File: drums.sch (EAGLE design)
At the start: 210 parts, among them IC1 4051N, IC3 7812T, IC5 OPA2134P, IC6 OPA4130P, IC7 LM2574HVN-5.0, IC8 74LS595N, J2 UBBS-4R-D14-4D

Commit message: added hihats, buncha stuff
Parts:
- added C49, C52, C56, C57, C64, C65: 15n, dan:C-US050-025X075
- added C50, C51: 10n, dan:C-US050-025X075
- added C53, C54: 12n, dan:C-US050-025X075
- added C55: 3.3n, dan:C-US050-025X075
- added C58, C62: 1u, dan:CPOL-USE2-5
- added C59: np, dan:C-US050-025X075
- added C60: .47u, dan:CPOL-USE2-5
- added C61: 5.6n, dan:C-US050-025X075
- added C63: np, dan:CPOL-USE2-5
- added C66: 33u, dan:CPOL-USE2-5
- added CHDECAY: 50k, dan:US-EVUF2J
- added D13, D14, D15, D16: 1N4148DO35-7, dan:1N4148DO35-7
- added HATFILTER, VOLUME: 10k, dan:US-EVUF2J
- added HATSLEVEL, OHDECAY1: 500k, dan:US-EVUF2J
- added IC2: 4584N, dan:4584N
- added IC9: OPA4130P, dan:OPA4130P
- added JP7, JP8: (no value), dan:PINHD-2X6
- added R101, R102, R103, R104, R105, R24: 150k, dan:R-US_0207/2V
- added R106: 1k, dan:R-US_0207/2V
- added R107, R131, R132, R133: 33k, dan:R-US_0207/2V
- added R108, R109: 100, dan:R-US_0207/2V
- added R110: 1M, dan:R-US_0207/2V
- added R111, R115, R123, R127: 22k, dan:R-US_0207/2V
- added R112, R130: 220, dan:R-US_0207/2V
- added R113, R118, R121, R126: 4.7k, dan:R-US_0207/2V
- added R114, R116, R117, R120, R122, R124, R125: 10k, dan:R-US_0207/2V
- added R119, R16, R20: 330k, dan:R-US_0207/2V
- added R128, R129, R134, R135, R136: 100k, dan:R-US_0207/2V
- added R137: 82k, dan:R-US_0207/2V
- added R19, R21: 470k, dan:R-US_0207/2V
- added R22, R23: 560k, dan:R-US_0207/2V
- added U$14, U$16, U$18, U$19, U$20, U$21, U$22: 2N3904_, dan:2N3904_
- added U$15, U$17: 2N3906_, dan:2N3906_
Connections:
- removed net N$132: JP1.6
- removed net N$138: JP2.4
- removed net N$144: JP2.3
- removed net N$145: JP2.5
- removed net N$2: R2.2, U$1.3.3V
- removed net N$32: JP1.3
- removed net N$35: R18.1, U$1.1/TX1/T
- removed net N$48: JP1.11
- removed net N$50: JP1.4
- new net CHDEC2A: CHDECAY.E
- new net CHDEC2B: C64.1, D13.A, JP2.5
- new net CHDEC3B: C60.+, D14.C, JP2.6
- new net CHDECA: CHDECAY.A, CHDECAY.S, JP1.4, JP1.6
- new net CHDECB: JP2.4, R119.2
- new net D+B: J2.D+, JP2.10
- new net D-B: J2.D-, JP2.11
- new net HATLEV2A: HATSLEVEL.A, JP1.9
- new net HATLEV2B: C66.-, JP2.9
- new net HATLEVA: HATSLEVEL.E, HATSLEVEL.S, JP1.8
- new net HATLEVB: IC9B.OUT, JP2.8, R134.1
- new net HFILTA: HATFILTER.E, JP1.3
- new net HFILTB: JP2.3, R108.2
- new net MIDRXA: JP1.12, U$1.0/RX1/T
- new net MIDRXB: JP2.12, OK1.VO, R2.1
- new net MIDTXA: JP1.5, U$1.1/TX1/T
- new net MIDTXB: JP2.7, R18.1
- new net N$106: IC2F.O, R105.2, R23.1
- new net N$107: C54.1, IC2F.I, R23.2
- new net N$109: C58.+, R110.2, U$14.B
- new net N$110: C55.2, R101.1, R102.1, R103.1, R104.1, R105.1, R106.1, R24.1
- new net N$143: C55.1, R107.2
- new net N$149: C56.2, IC9A.-IN, R107.1, R137.2
- new net N$150: C56.1, C57.2, R108.1
- new net N$151: C57.1, C58.-, IC9A.OUT, R137.1
- new net N$152: R109.1, U$14.E
- new net N$155: C59.1, D13.C, D15.C, U$14.C
- new net N$156: JP8.12
- new net N$158: D14.A, R112.1
- new net N$159: R113.1, R114.2, U$15.B
- new net N$161: R111.2, R112.2, U$15.C
- new net N$162: R113.2, R117.1, R118.1, U$15.E
- new net N$163: R114.1, U$16.C
- new net N$164: R115.1, R116.1, U$16.B
- new net N$168: D16.A, R127.2, U$17.C
- new net N$169: R121.1, R122.2, U$17.B
- new net N$170: R121.2, R125.1, R126.1, U$17.E
- new net N$171: R122.1, U$18.C
- new net N$173: R123.1, R124.1, U$18.B
- new net N$176: R120.2, R127.1, U$19.B
- new net N$177: C61.1, R128.2, U$19.C
- new net N$178: C65.1, D15.A, R133.1
- new net N$179: R128.1, U$20.B
- new net N$180: C63.+, R129.2, U$20.C, U$21.C
- new net N$181: D16.C, R130.2
- new net N$183: R131.1, U$22.B
- new net N$184: R132.2, R133.2, U$22.E
- new net N$185: R119.1, U$21.B
- new net N$187: C64.2, R136.2
- new net N$188: C65.2, R135.2
- new net N$189: C66.+, IC9B.-IN, R134.2, R135.1, R136.1
- new net N$31: C52.1, IC2D.I, R21.2
- new net N$49: IC2D.O, R103.2, R21.1
- new net N$67: IC2A.O, R16.1, R24.2
- new net N$71: C49.1, IC2A.I, R16.2
- new net N$74: C50.1, IC2B.I, R19.2
- new net N$75: IC2B.O, R101.2, R19.1
- new net N$79: IC2C.O, R102.2, R20.1
- new net N$80: C51.1, IC2C.I, R20.2
- new net N$85: C53.1, IC2E.I, R22.2
- new net N$86: IC2E.O, R104.2, R22.1
- new net OHDECA: JP7.2, OHDECAY1.A
- new net OHDECB: C62.+, JP8.2, R129.1, R130.1, R131.2
- new net T5B: JP8.3, R115.2
- new net T6B: JP8.4, R123.2
- new net T7B: JP8.5, R118.2, R126.2
- net +12V: now also IC9A.V+, R110.1, R117.2, R125.2, U$22.C
- net -12V: now also IC9A.V-
- net 3.3V: now also IC1P.VCC, IC2P.VDD, U$1.3.3V; no longer OK1.VO, R2.1, U$1.0/RX1/T
- net 5V: now also IC8P.VCC, R2.2
- net D+A: now also JP1.10; no longer J2.D+
- net D-A: now also JP1.11; no longer J2.D-
- net GND: now also C49.2, C50.2, C51.2, C52.2, C53.2, C54.2, C59.2, C60.-, C61.2, C62.-, C63.-, HATFILTER.A, HATFILTER.S, IC1P.GND, IC1P.VEE, IC2P.VSS, IC8P.GND, IC9A.+IN, IC9B.+IN, JP1.7, JP7.1, JP8.1, OHDECAY1.E, OHDECAY1.S, R106.2, R109.2, R111.1, R116.2, R120.1, R124.2, R132.1, U$16.E, U$18.E, U$19.E, U$20.E, U$21.E
- net N$134: now also JP8.7; no longer JP1.8
- net N$135: now also JP8.9; no longer JP1.10
- net N$136: now also JP8.11; no longer JP1.12
- net N$139: now also JP7.6; no longer JP2.6
- net N$140: now also JP7.8; no longer JP2.8
- net N$141: now also JP7.10; no longer JP2.10
- net N$142: now also JP7.12; no longer JP2.12
- net N$146: now also JP8.6; no longer JP2.7
- net N$147: now also JP8.8; no longer JP2.9
- net N$148: now also JP8.10; no longer JP2.11
- net N$38: now also JP7.7; no longer JP1.5
- net N$39: now also JP7.9; no longer JP1.7
- net N$47: now also JP7.11; no longer JP1.9
- net T5: now also JP7.3
- net T6: now also JP7.4
- net T7: now also JP7.5
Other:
- note added: "maybe patch in noise here too"
- moved on the sheet: C7, D+, D-, R2, R25

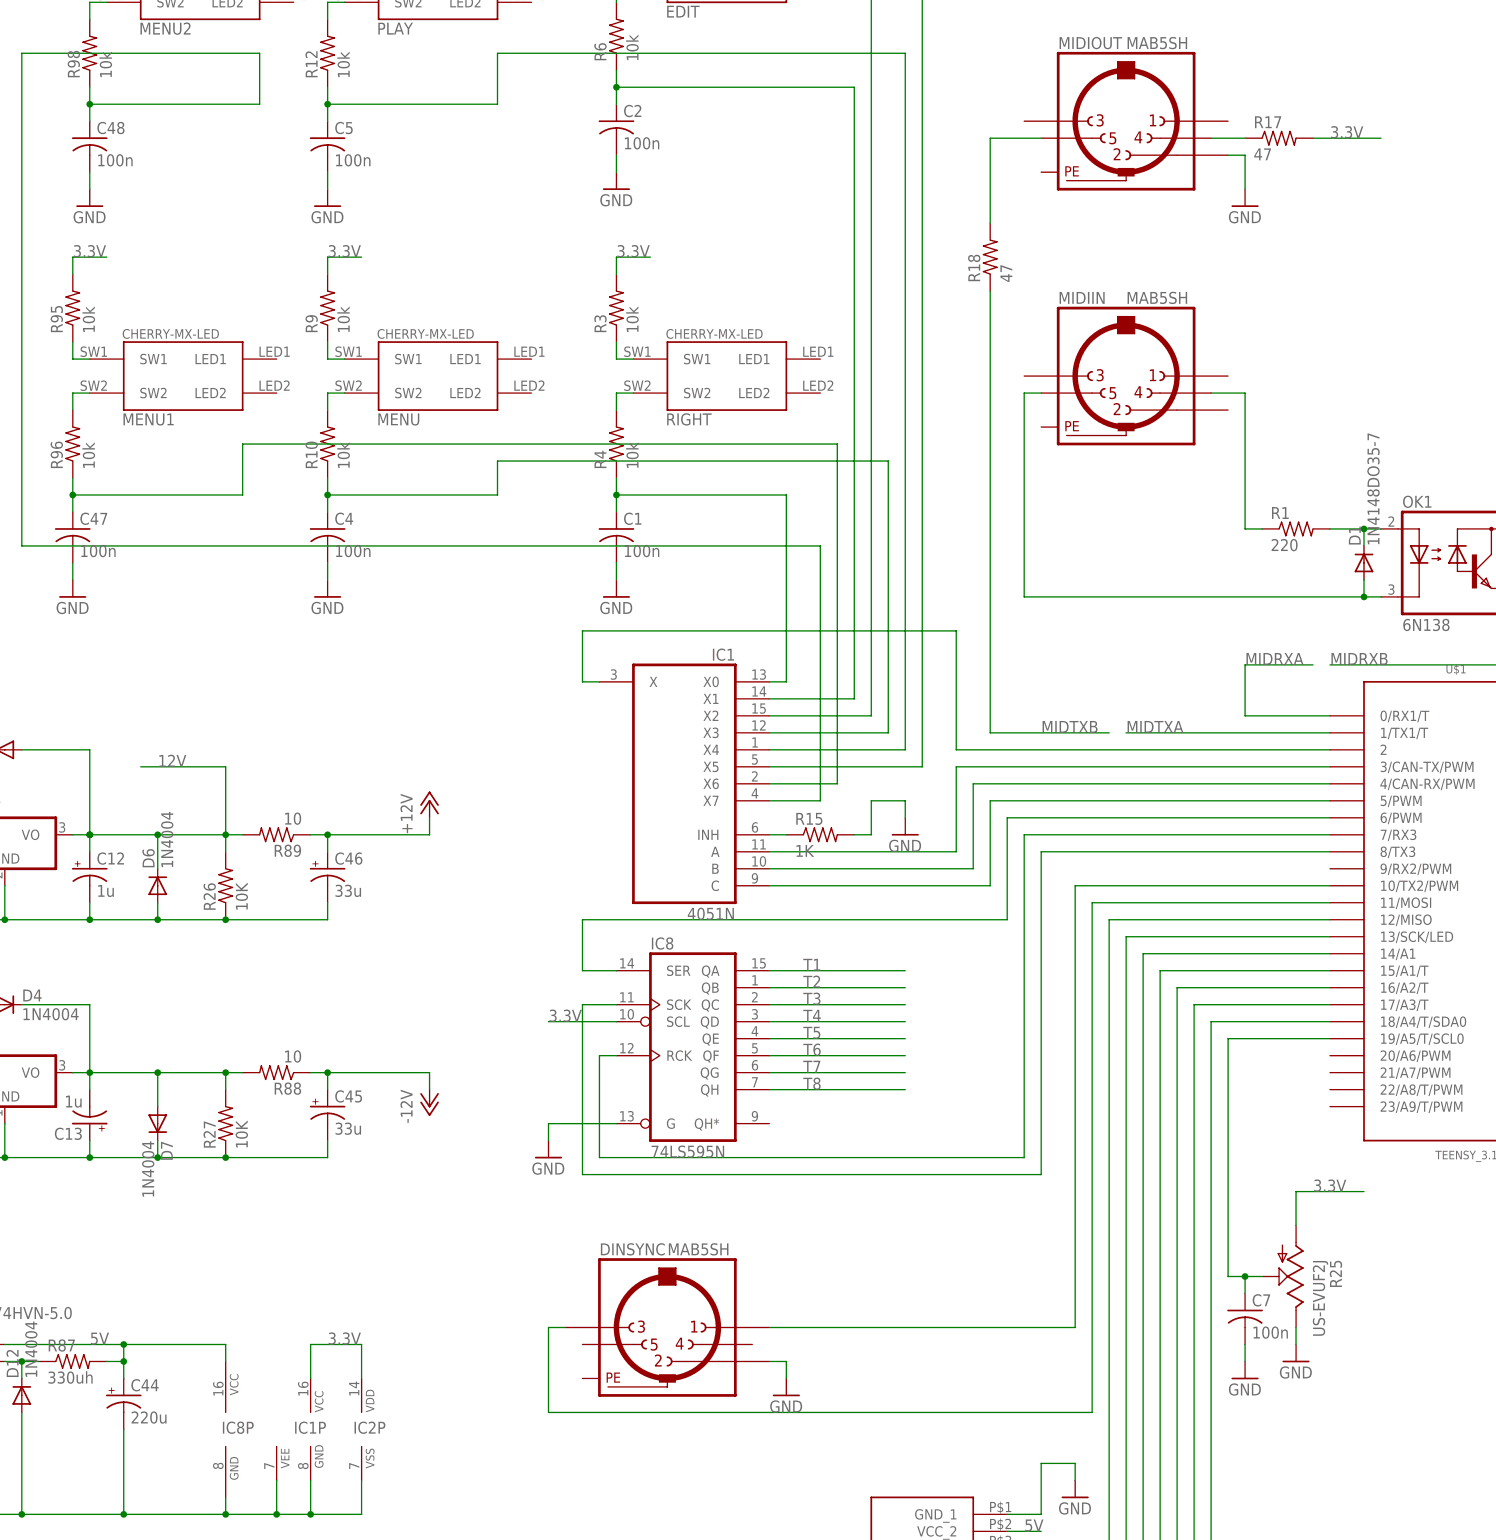
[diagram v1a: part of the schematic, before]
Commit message: made hihat layout
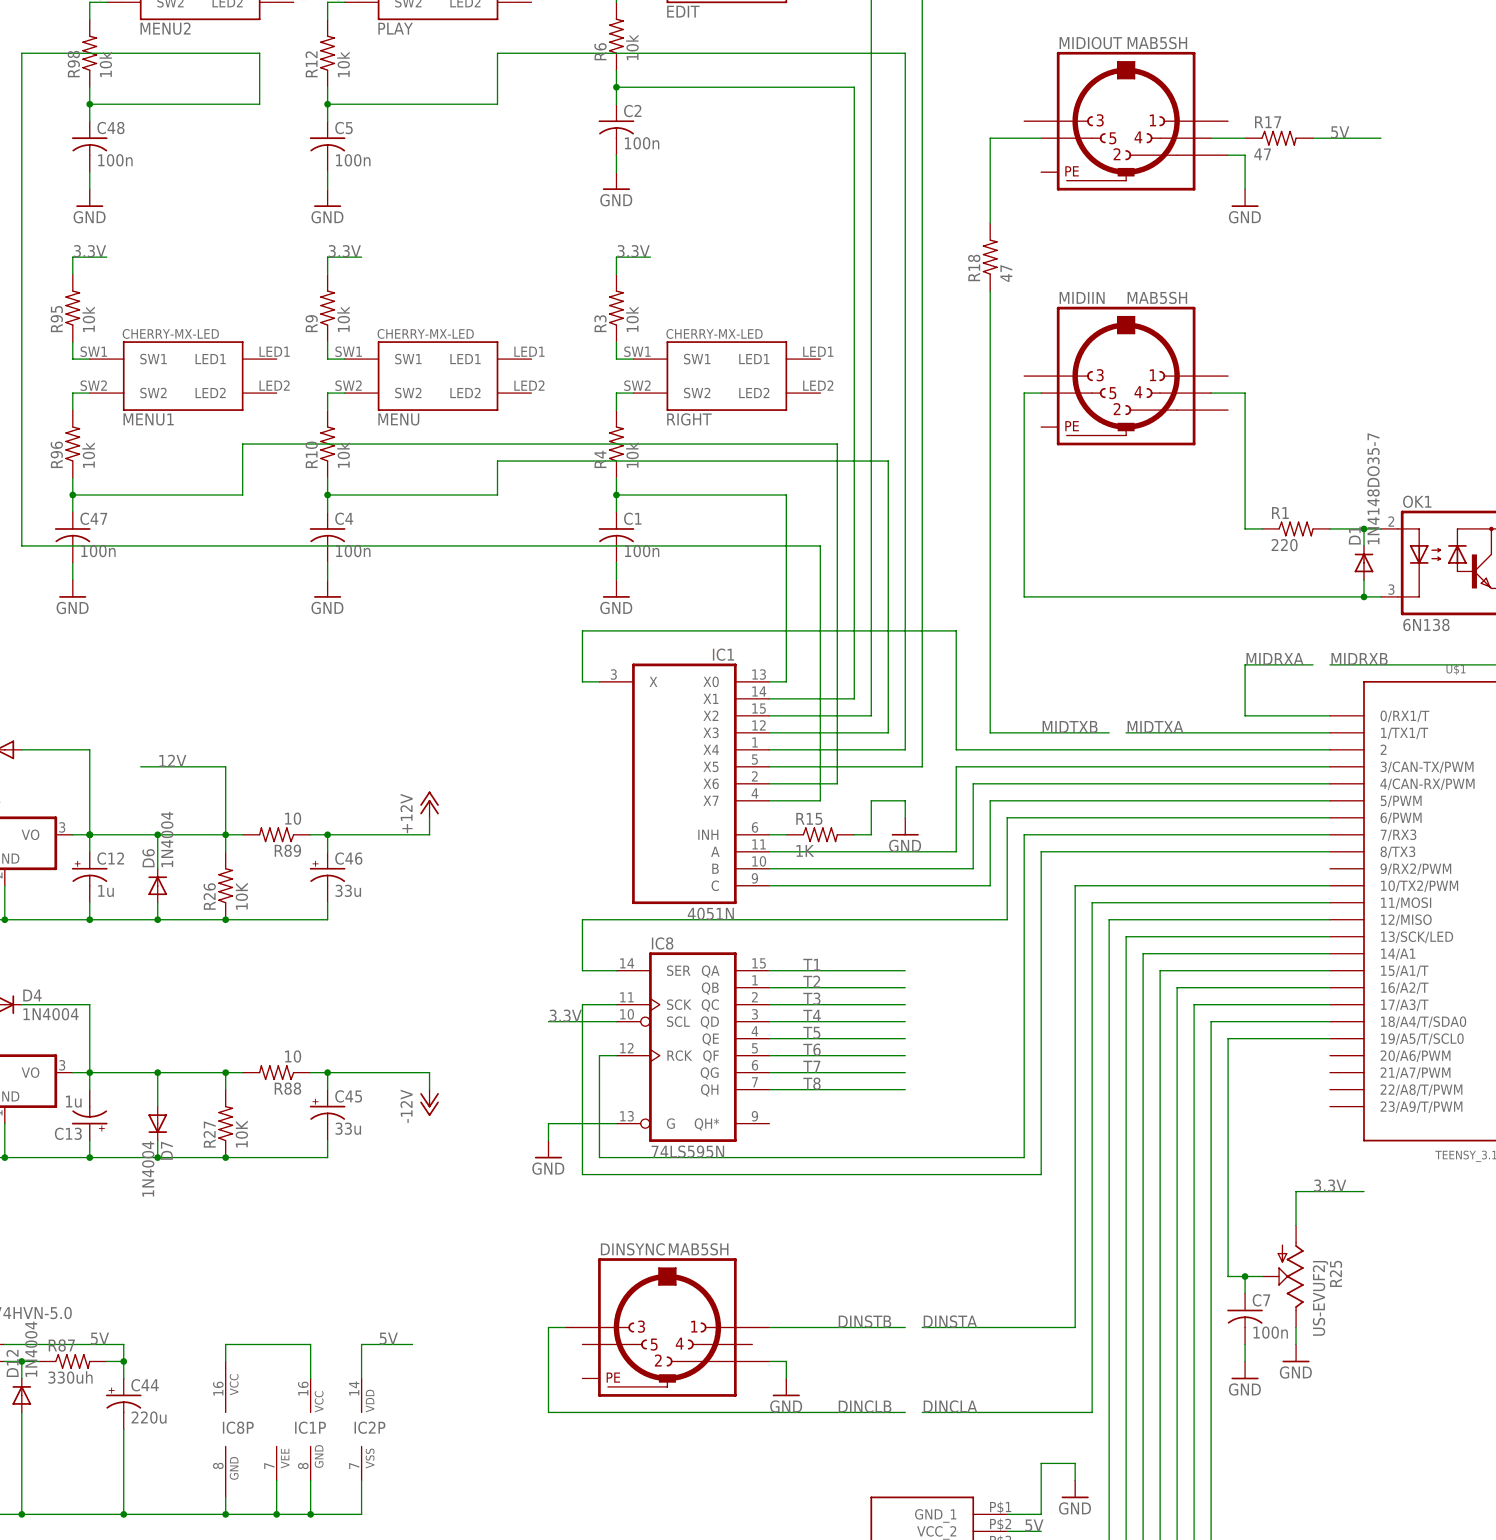
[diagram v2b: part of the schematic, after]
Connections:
- removed net N$36: DINSYNC.1, U$1.10/TX2/PWM
- removed net N$37: DINSYNC.3, U$1.11/MOSI
- new net DINCLA: U$1.11/MOSI
- new net DINCLB: DINSYNC.3
- new net DINSTA: U$1.10/TX2/PWM
- new net DINSTB: DINSYNC.1
- net 3.3V: now also IC8P.VCC; no longer IC2P.VDD, R17.2
- net 5V: now also IC2P.VDD, R17.2; no longer IC8P.VCC
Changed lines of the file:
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@@
 </segment>
 <segment>
-<pinref part="R17" gate="G$1" pin="2"/>
-<wire x1="30.48" y1="236.22" x2="40.64" y2="236.22" width="0.1524" layer="91"/>
-<label x="33.02" y="236.22" size="1.778" layer="95"/>
-</segment>
-<segment>
 <pinref part="R25" gate="G$1" pin="A"/>
 <wire x1="27.94" y1="73.66" x2="27.94" y2="78.74" width="0.1524" layer="91"/>
@@
 </segment>
 <segment>
-<pinref part="IC2" gate="P" pin="VDD"/>
 <pinref part="IC1" gate="P" pin="VCC"/>
 <wire x1="-119.38" y1="50.8" x2="-119.38" y2="55.88" width="0.1524" layer="91"/>
-<wire x1="-119.38" y1="55.88" x2="-111.76" y2="55.88" width="0.1524" layer="91"/>
-<wire x1="-111.76" y1="55.88" x2="-111.76" y2="50.8" width="0.1524" layer="91"/>
-<label x="-116.84" y="55.88" size="1.778" layer="95"/>
+<pinref part="IC8" gate="P" pin="VCC"/>
+<wire x1="-132.08" y1="53.34" x2="-132.08" y2="55.88" width="0.1524" layer="91"/>
+<wire x1="-119.38" y1="55.88" x2="-132.08" y2="55.88" width="0.1524" layer="91"/>
 </segment>
 <segment>
@@
 <net name="5V" class="0">
 <segment>
-<pinref part="U$1" gate="G$1" pin="VIN"/>
-<wire x1="78.74" y1="149.86" x2="86.36" y2="149.86" width="0.1524" layer="91"/>
-<wire x1="86.36" y1="149.86" x2="86.36" y2="177.8" width="0.1524" layer="91"/>
-<pinref part="OK1" gate="G$1" pin="VCC"/>
-<wire x1="86.36" y1="177.8" x2="76.2" y2="177.8" width="0.1524" layer="91"/>
-<label x="73.66" y="177.8" size="1.778" layer="95"/>
-<pinref part="R2" gate="G$1" pin="2"/>
-<wire x1="76.2" y1="177.8" x2="66.04" y2="177.8" width="0.1524" layer="91"/>
-<wire x1="76.2" y1="175.26" x2="76.2" y2="177.8" width="0.1524" layer="91"/>
-<junction x="76.2" y="177.8"/>
-</segment>
-<segment>
 <pinref part="R87" gate="G$1" pin="2"/>
 <wire x1="-149.86" y1="53.34" x2="-147.32" y2="53.34" width="0.1524" layer="91"/>
@@
 <junction x="-147.32" y="53.34"/>
 <label x="-152.4" y="55.88" size="1.778" layer="95"/>
-<wire x1="-147.32" y1="55.88" x2="-132.08" y2="55.88" width="0.1524" layer="91"/>
-<pinref part="IC8" gate="P" pin="VCC"/>
-<wire x1="-132.08" y1="53.34" x2="-132.08" y2="55.88" width="0.1524" layer="91"/>
-<junction x="-147.32" y="55.88"/>
 </segment>
 <segment>
@@
 <label x="-12.7" y="27.94" size="1.778" layer="95"/>
 </segment>
+<segment>
+<pinref part="IC2" gate="P" pin="VDD"/>
+<wire x1="-111.76" y1="55.88" x2="-111.76" y2="50.8" width="0.1524" layer="91"/>
+<wire x1="-111.76" y1="55.88" x2="-104.14" y2="55.88" width="0.1524" layer="91"/>
+<label x="-109.22" y="55.88" size="1.778" layer="95"/>
+</segment>
+<segment>
+<pinref part="U$1" gate="G$1" pin="VIN"/>
+<wire x1="78.74" y1="149.86" x2="86.36" y2="149.86" width="0.1524" layer="91"/>
+<wire x1="86.36" y1="149.86" x2="86.36" y2="177.8" width="0.1524" layer="91"/>
+<pinref part="OK1" gate="G$1" pin="VCC"/>
+<wire x1="86.36" y1="177.8" x2="76.2" y2="177.8" width="0.1524" layer="91"/>
+<label x="73.66" y="177.8" size="1.778" layer="95"/>
+<pinref part="R2" gate="G$1" pin="2"/>
+<wire x1="76.2" y1="177.8" x2="66.04" y2="177.8" width="0.1524" layer="91"/>
+<wire x1="76.2" y1="175.26" x2="76.2" y2="177.8" width="0.1524" layer="91"/>
+<junction x="76.2" y="177.8"/>
+</segment>
+<segment>
+<pinref part="R17" gate="G$1" pin="2"/>
+<wire x1="30.48" y1="236.22" x2="40.64" y2="236.22" width="0.1524" layer="91"/>
+<label x="33.02" y="236.22" size="1.778" layer="95"/>
+</segment>
 </net>
 <net name="N$4" class="0">
@@
 </segment>
 </net>
-<net name="N$36" class="0">
+<net name="DINSTA" class="0">
 <segment>
-<pinref part="DINSYNC" gate="G$1" pin="1"/>
-<wire x1="-50.8" y1="58.42" x2="-5.08" y2="58.42" width="0.1524" layer="91"/>
 <wire x1="-5.08" y1="58.42" x2="-5.08" y2="124.46" width="0.1524" layer="91"/>
 <pinref part="U$1" gate="G$1" pin="10/TX2/PWM"/>
 <wire x1="-5.08" y1="124.46" x2="33.02" y2="124.46" width="0.1524" layer="91"/>
+<wire x1="-5.08" y1="58.42" x2="-27.94" y2="58.42" width="0.1524" layer="91"/>
+<label x="-27.94" y="58.42" size="1.778" layer="95"/>
 </segment>
 </net>
-<net name="N$37" class="0">
+<net name="DINCLA" class="0">
 <segment>
-<pinref part="DINSYNC" gate="G$1" pin="3"/>
-<wire x1="-81.28" y1="58.42" x2="-83.82" y2="58.42" width="0.1524" layer="91"/>
-<wire x1="-83.82" y1="58.42" x2="-83.82" y2="45.72" width="0.1524" layer="91"/>
-<wire x1="-83.82" y1="45.72" x2="-2.54" y2="45.72" width="0.1524" layer="91"/>
 <wire x1="-2.54" y1="45.72" x2="-2.54" y2="121.92" width="0.1524" layer="91"/>
 <pinref part="U$1" gate="G$1" pin="11/MOSI"/>
 <wire x1="-2.54" y1="121.92" x2="33.02" y2="121.92" width="0.1524" layer="91"/>
+<wire x1="-2.54" y1="45.72" x2="-27.94" y2="45.72" width="0.1524" layer="91"/>
+<label x="-27.94" y="45.72" size="1.778" layer="95"/>
 </segment>
 </net>
@@
 </segment>
 </net>
+<net name="DINCLB" class="0">
+<segment>
+<label x="-40.64" y="45.72" size="1.778" layer="95"/>
+<wire x1="-83.82" y1="45.72" x2="-30.48" y2="45.72" width="0.1524" layer="91"/>
+<wire x1="-83.82" y1="58.42" x2="-83.82" y2="45.72" width="0.1524" layer="91"/>
+<pinref part="DINSYNC" gate="G$1" pin="3"/>
+<wire x1="-81.28" y1="58.42" x2="-83.82" y2="58.42" width="0.1524" layer="91"/>
+</segment>
+</net>
+<net name="DINSTB" class="0">
+<segment>
+<pinref part="DINSYNC" gate="G$1" pin="1"/>
+<wire x1="-50.8" y1="58.42" x2="-30.48" y2="58.42" width="0.1524" layer="91"/>
+<label x="-40.64" y="58.42" size="1.778" layer="95"/>
+</segment>
+</net>
